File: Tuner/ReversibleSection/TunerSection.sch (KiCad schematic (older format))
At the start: 97 parts, among them J1 Conn_01x03, J10 Conn_01x02, J11 Conn_01x05, J12 Conn_01x01, J13 Conn_01x01, J14 Conn_01x01, J15 Conn_01x01, J2 Conn_01x03, J3 Conn_01x03, J4 Conn_01x03, J5 Conn_01x03, J6 Conn_01x03, J7 Conn_01x03, J8 Conn_01x02, J9 Conn_01x02, P10 Conn_01x01, P11 Conn_01x01, P12 Conn_01x01, P2 Conn_01x01, P3 Conn_01x01, P4 Conn_01x01, P5 Conn_01x01, P6 Conn_01x01, P7 Conn_01x01, P8 Conn_01x01, P9 Conn_01x01, U1 MCP23008, U2 ULN2803A

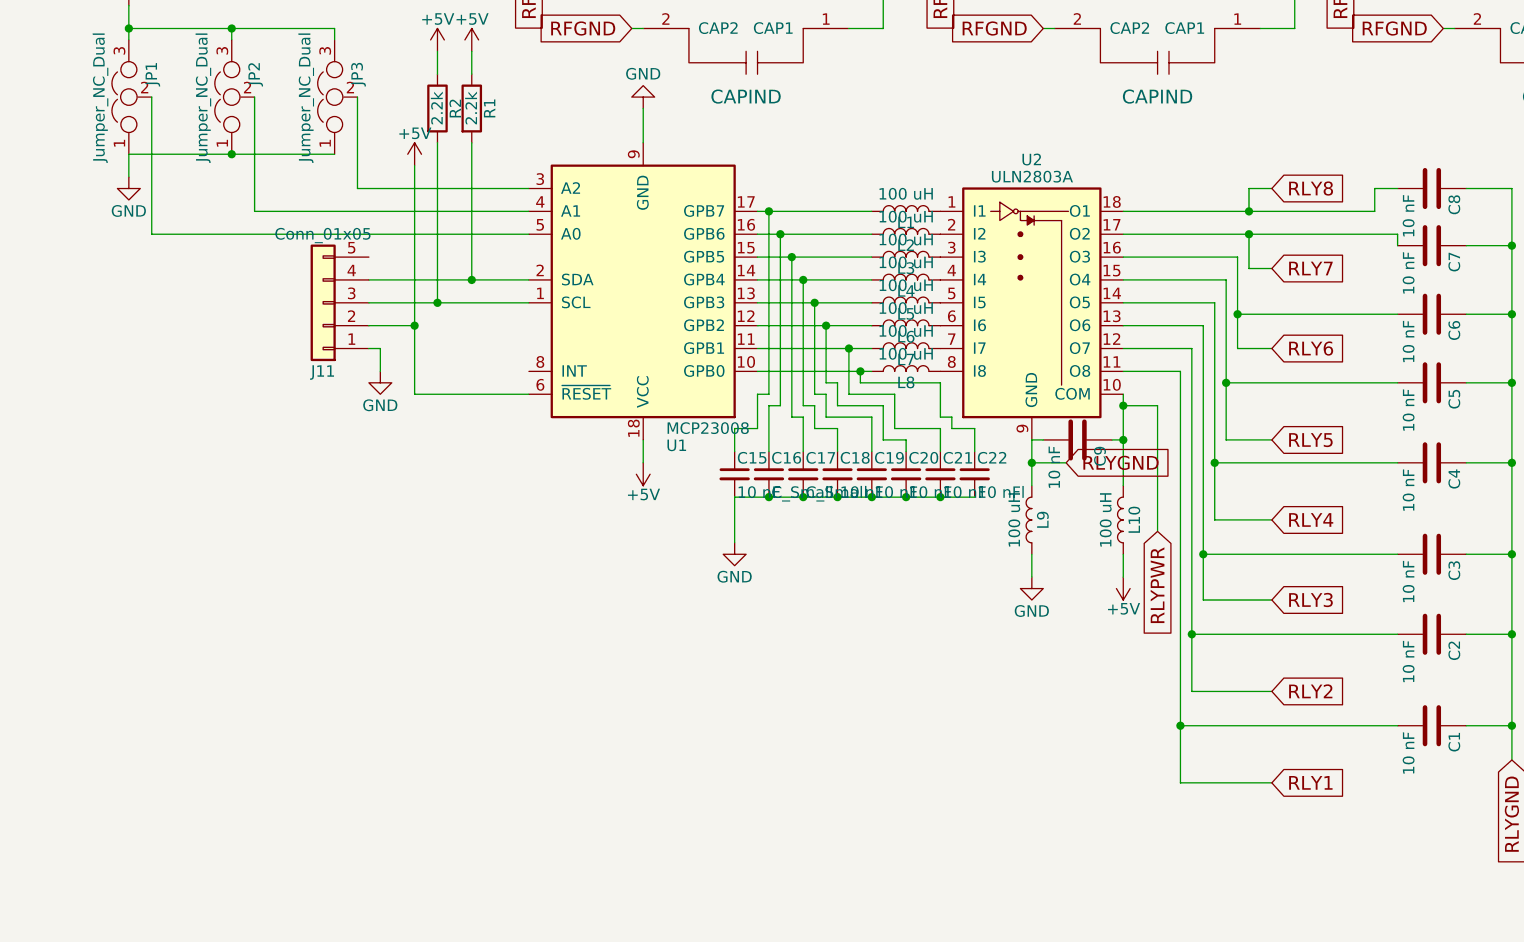
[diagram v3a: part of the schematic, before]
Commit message: JLCPCB order 09232018 - improved grounding - improved I2C cabling - NEO7M port - support for common mode chokes - relay board now has capacitors on all coils
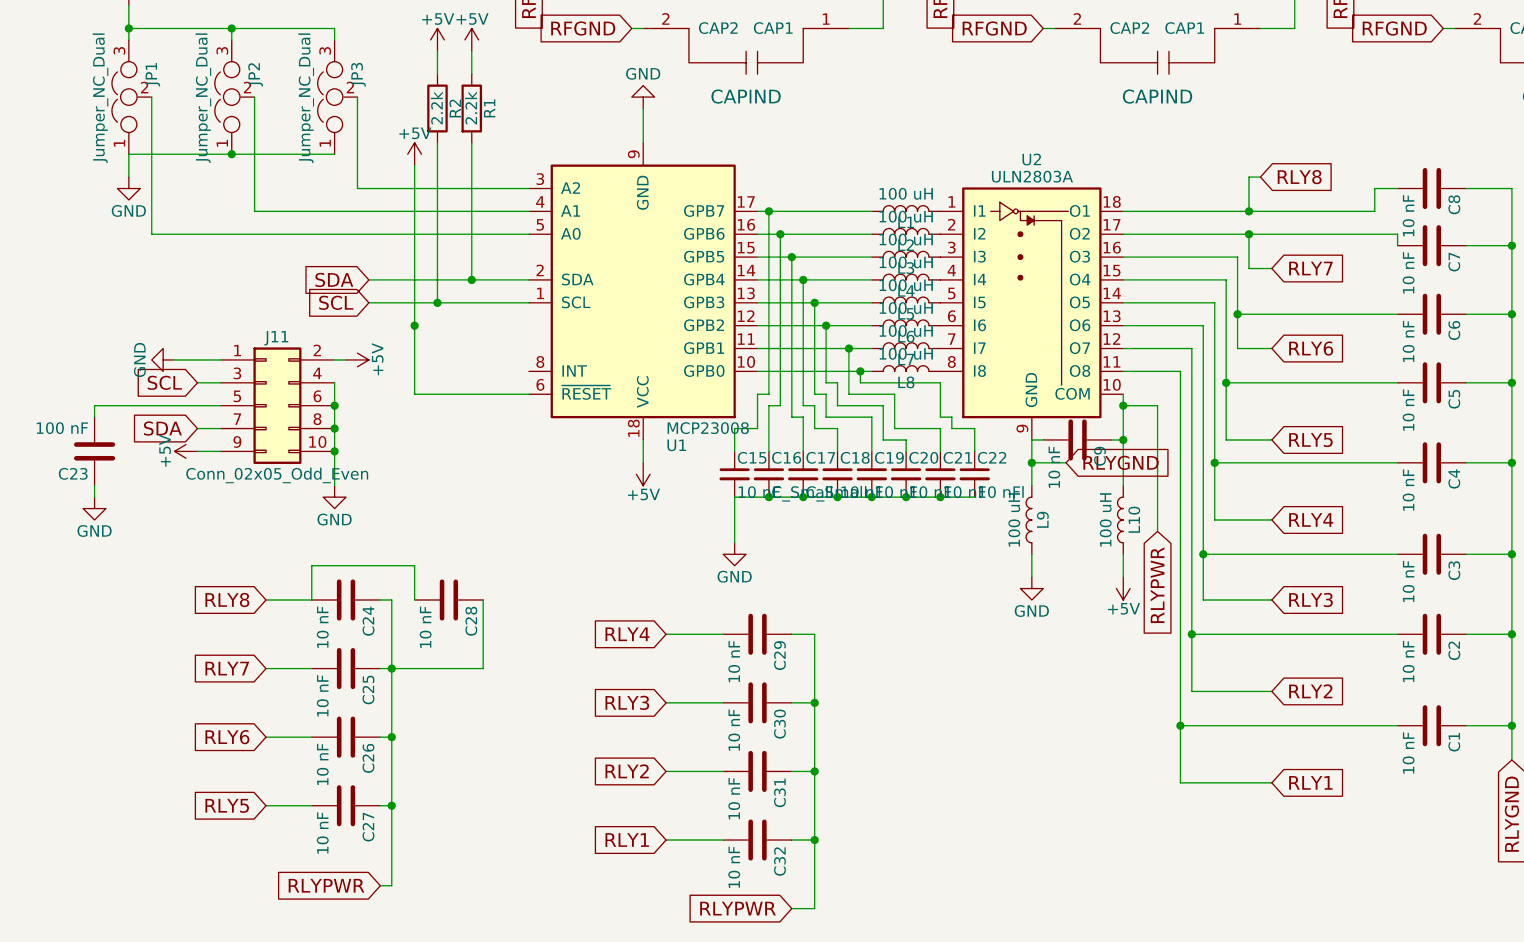
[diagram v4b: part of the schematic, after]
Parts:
- removed J11: Conn_01x05, Connectors_Molex:Molex_KK-6410-05_05x2.54mm_Straight, symbol Conn_01x05
- added C23: 100 nF, Capacitors_THT:C_Disc_D5.0mm_W2.5mm_P2.50mm, symbol C
- added C24, C25, C26, C27, C28, C29, C30, C31, C32: 10 nF, Capacitors_THT:C_Disc_D5.0mm_W2.5mm_P2.50mm, symbol C
- added J11: Conn_02x05_Odd_Even, Pin_Headers:Pin_Header_Straight_2x05_Pitch2.54mm, symbol Conn_02x05_Odd_Even
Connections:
- net +5V: now also J11.2 (Pin_2), J11.9 (Pin_9)
- net GND: now also C23.1, J11.1 (Pin_1), J11.10 (Pin_10), J11.4 (Pin_4), J11.6 (Pin_6), J11.8 (Pin_8)
- net RLY1: now also C32.2
- net RLY2: now also C31.2
- net RLY3: now also C30.2
- net RLY4: now also C29.2
- net RLY5: now also C27.2
- net RLY6: now also C26.2
- net RLY7: now also C25.2
- net RLY8: now also C24.2, C28.2
- net RLYPWR: now also C24.1, C25.1, C26.1, C27.1, C28.1, C29.1, C30.1, C31.1, C32.1
- net SCL: now reaches R2.2, U1.1 (SCL)
- net SCL: now also J11.3 (Pin_3)
- net SDA: now reaches R1.2, U1.2 (SDA)
- net SDA: now also J11.7 (Pin_7)
- new net: C23.2, J11.5 (Pin_5)

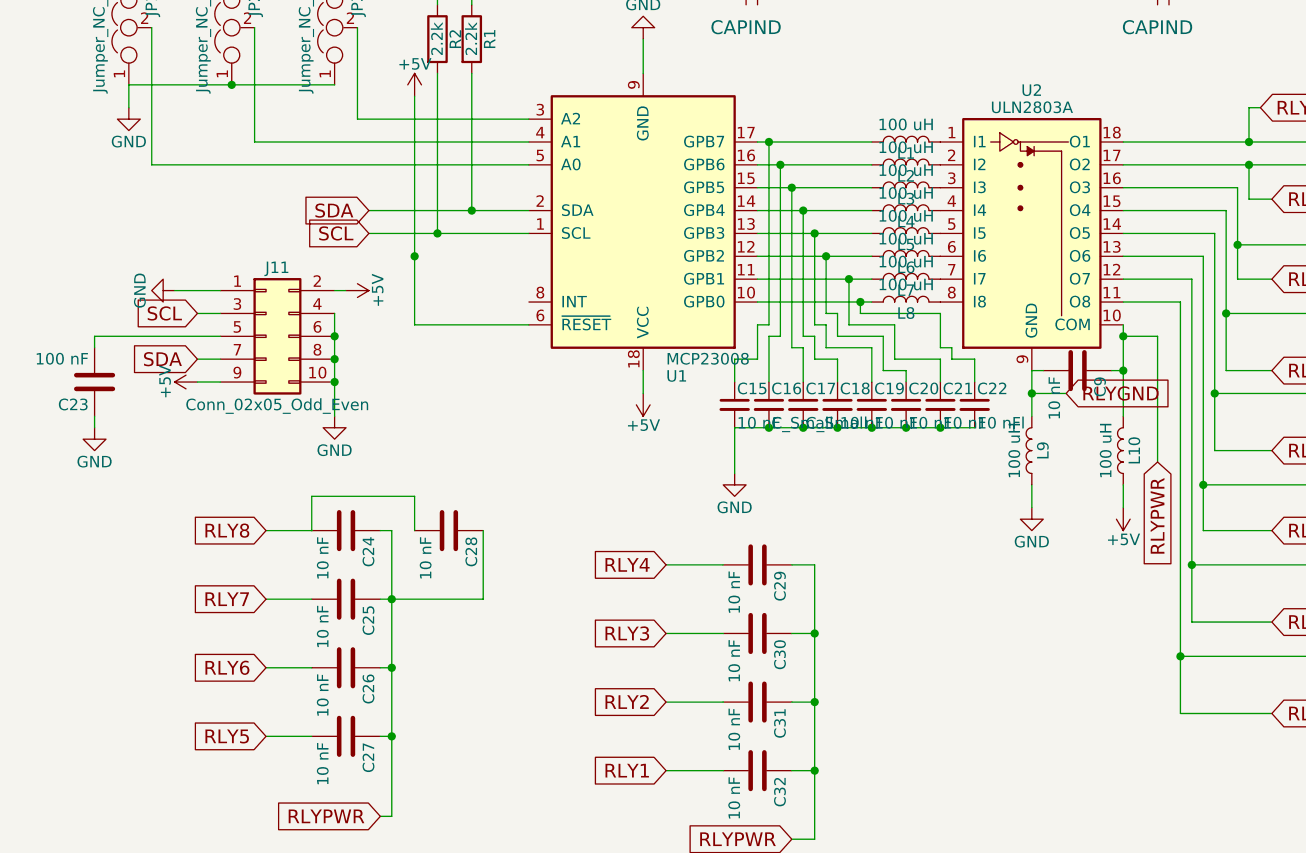
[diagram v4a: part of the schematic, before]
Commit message: Relay boards changed to have coil terminals all on same side
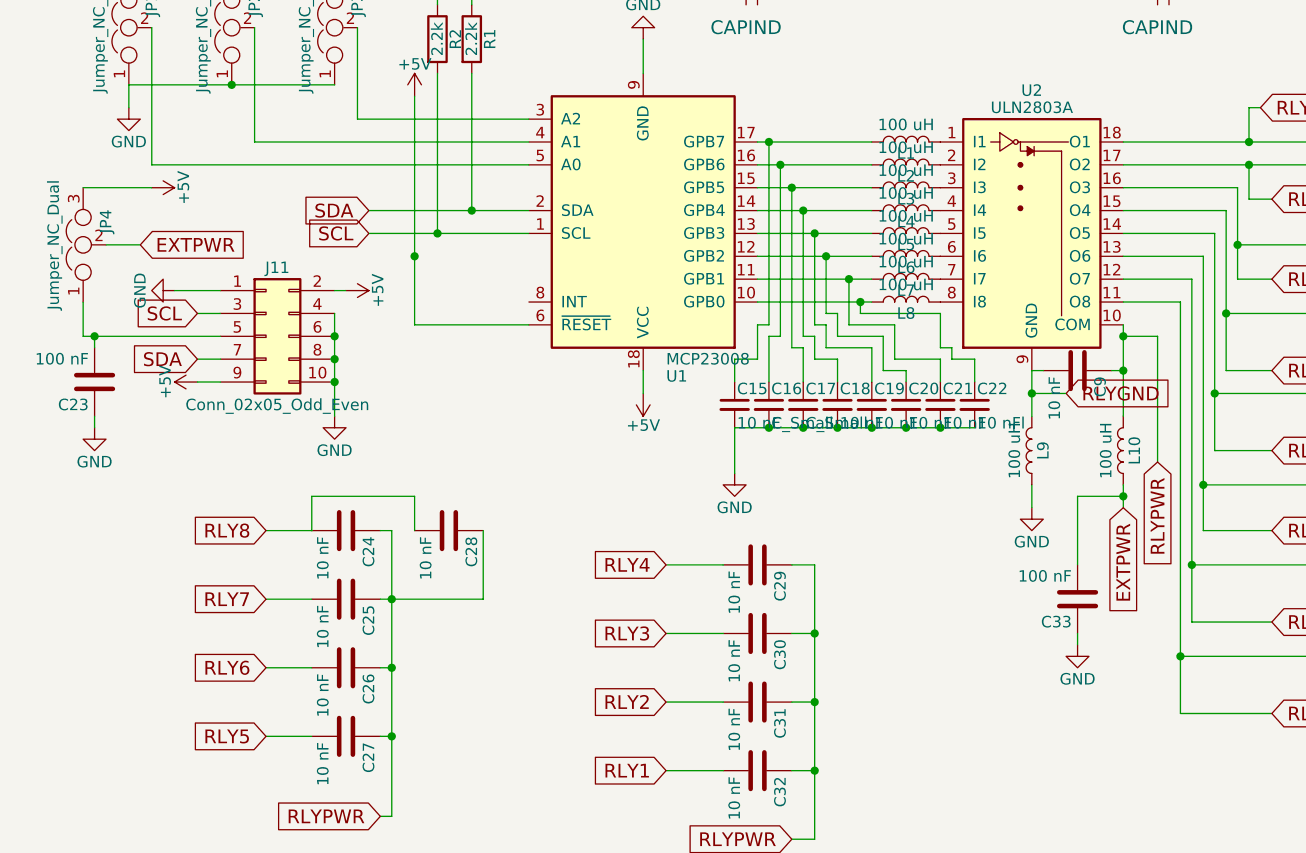
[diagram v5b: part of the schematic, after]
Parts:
- added C33: 100 nF, Capacitors_THT:C_Disc_D5.0mm_W2.5mm_P2.50mm, symbol C
- added JP4: Jumper_NC_Dual, Pin_Headers:Pin_Header_Straight_1x03_Pitch2.54mm, symbol Jumper_NC_Dual
- C11: footprint Capacitors_THT:CP_Radial_D8.0mm_P5.00mm -> Capacitors_THT:CP_Radial_Tantal_D5.0mm_P2.50mm
- C14, C9: footprint Capacitors_THT:C_Disc_D5.0mm_W2.5mm_P2.50mm -> Capacitors_THT:C_Disc_D5.0mm_W2.5mm_P5.00mm
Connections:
- net +5V: now also JP4.3; no longer L10.1
- net GND: now also C33.1
- net at C23.2, J11.5 (Pin_5): now also JP4.1
- new net EXTPWR: C33.2, JP4.2, L10.1
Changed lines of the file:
@@
 RLY8
 $Comp
-L +5V #PWR12
+L +5V #PWR13
 U 1 1 5B1A0287
 P 3150 5750
-F 0 "#PWR12" H 3150 5600 50  0001 C CNN
+F 0 "#PWR13" H 3150 5600 50  0001 C CNN
 F 1 "+5V" H 3150 5890 50  0000 C CNN
 F 2 "" H 3150 5750 50  0001 C CNN
@@
 $EndComp
 $Comp
-L +5V #PWR8
+L +5V #PWR9
 U 1 1 5B1ABA5A
 P 2150 4450
-F 0 "#PWR8" H 2150 4300 50  0001 C CNN
+F 0 "#PWR9" H 2150 4300 50  0001 C CNN
 F 1 "+5V" H 2150 4590 50  0000 C CNN
 F 2 "" H 2150 4450 50  0001 C CNN
@@
 $EndComp
 $Comp
-L +5V #PWR10
+L +5V #PWR11
 U 1 1 5B1ABCDE
 P 2400 3950
-F 0 "#PWR10" H 2400 3800 50  0001 C CNN
+F 0 "#PWR11" H 2400 3800 50  0001 C CNN
 F 1 "+5V" H 2400 4090 50  0000 C CNN
 F 2 "" H 2400 3950 50  0001 C CNN
@@
 $EndComp
 $Comp
-L +5V #PWR16
+L +5V #PWR17
 U 1 1 5B1ABFC6
 P 8800 4600
-F 0 "#PWR16" H 8800 4450 50  0001 C CNN
+F 0 "#PWR17" H 8800 4450 50  0001 C CNN
 F 1 "+5V" H 8800 4740 50  0000 C CNN
 F 2 "" H 8800 4600 50  0001 C CNN
@@
 $EndComp
 $Comp
-L GND #PWR17
+L GND #PWR18
 U 1 1 5B1AC04C
 P 8800 5050
-F 0 "#PWR17" H 8800 4800 50  0001 C CNN
+F 0 "#PWR18" H 8800 4800 50  0001 C CNN
 F 1 "GND" H 8800 4900 50  0000 C CNN
 F 2 "" H 8800 5050 50  0001 C CNN
@@
 F 0 "C11" H 9525 4950 50  0000 L CNN
 F 1 "100 uF" H 9525 4750 50  0000 L CNN
-F 2 "Capacitors_THT:CP_Radial_D8.0mm_P5.00mm" H 9538 4700 50  0001 C CNN
+F 2 "Capacitors_THT:CP_Radial_Tantal_D5.0mm_P2.50mm" H 9538 4700 50  0001 C CNN
 F 3 "" H 9500 4850 50  0001 C CNN
 	1    9500 4850
@@
 $EndComp
 $Comp
-L +5V #PWR9
+L +5V #PWR10
 U 1 1 5B196BCE
 P 2250 3950
-F 0 "#PWR9" H 2250 3800 50  0001 C CNN
+F 0 "#PWR10" H 2250 3800 50  0001 C CNN
 F 1 "+5V" H 2250 4090 50  0000 C CNN
 F 2 "" H 2250 3950 50  0001 C CNN
@@
 $EndComp
 $Comp
-L GND #PWR14
+L GND #PWR15
 U 1 1 5B9A4AE1
 P 4850 6250
-F 0 "#PWR14" H 4850 6000 50  0001 C CNN
+F 0 "#PWR15" H 4850 6000 50  0001 C CNN
 F 1 "GND" H 4850 6100 50  0000 C CNN
 F 2 "" H 4850 6250 50  0001 C CNN
@@
 	1    4850 6250
 	1    0    0    -1
-$EndComp
-$Comp
-L +5V #PWR15
-U 1 1 5B9A4F6D
-P 5250 6250
-F 0 "#PWR15" H 5250 6100 50  0001 C CNN
-F 1 "+5V" H 5250 6390 50  0000 C CNN
-F 2 "" H 5250 6250 50  0001 C CNN
-F 3 "" H 5250 6250 50  0001 C CNN
-	1    5250 6250
-	-1   0    0    1
 $EndComp
 $Comp
@@
 $EndComp
 $Comp
-L GND #PWR11
+L GND #PWR12
 U 1 1 5B9A6036
 P 3150 4200
-F 0 "#PWR11" H 3150 3950 50  0001 C CNN
+F 0 "#PWR12" H 3150 3950 50  0001 C CNN
 F 1 "GND" H 3150 4050 50  0000 C CNN
 F 2 "" H 3150 4200 50  0001 C CNN
@@
 $EndComp
 $Comp
-L GND #PWR13
+L GND #PWR14
 U 1 1 5B9ACA36
 P 3550 6100
-F 0 "#PWR13" H 3550 5850 50  0001 C CNN
+F 0 "#PWR14" H 3550 5850 50  0001 C CNN
 F 1 "GND" H 3550 5950 50  0000 C CNN
 F 2 "" H 3550 6100 50  0001 C CNN
@@
 F 0 "C9" H 5075 5750 50  0000 L CNN
 F 1 "10 nF" H 5075 5550 50  0000 L CNN
-F 2 "Capacitors_THT:C_Disc_D5.0mm_W2.5mm_P2.50mm" H 5088 5500 50  0001 C CNN
+F 2 "Capacitors_THT:C_Disc_D5.0mm_W2.5mm_P5.00mm" H 5088 5500 50  0001 C CNN
 F 3 "" H 5050 5650 50  0001 C CNN
 	1    5050 5650
@@
 $EndComp
 $Comp
-L GND #PWR18
+L GND #PWR19
 U 1 1 5B982525
 P 9850 2000
-F 0 "#PWR18" H 9850 1750 50  0001 C CNN
+F 0 "#PWR19" H 9850 1750 50  0001 C CNN
 F 1 "GND" H 9850 1850 50  0000 C CNN
 F 2 "" H 9850 2000 50  0001 C CNN
@@
 F 0 "C14" H 10175 2350 50  0000 L CNN
 F 1 "10 nF" H 10175 2150 50  0000 L CNN
-F 2 "Capacitors_THT:C_Disc_D5.0mm_W2.5mm_P2.50mm" H 10188 2100 50  0001 C CNN
+F 2 "Capacitors_THT:C_Disc_D5.0mm_W2.5mm_P5.00mm" H 10188 2100 50  0001 C CNN
 F 3 "" H 10150 2250 50  0001 C CNN
 	1    10150 2250
@@
 $EndComp
 $Comp
-L GND #PWR6
+L GND #PWR7
 U 1 1 5BA4D8F3
 P 1800 5850
-F 0 "#PWR6" H 1800 5600 50  0001 C CNN
+F 0 "#PWR7" H 1800 5600 50  0001 C CNN
 F 1 "GND" H 1800 5700 50  0000 C CNN
 F 2 "" H 1800 5850 50  0001 C CNN
@@
 $EndComp
 $Comp
-L +5V #PWR7
+L +5V #PWR8
 U 1 1 5BA4E273
 P 1850 5300
-F 0 "#PWR7" H 1850 5150 50  0001 C CNN
+F 0 "#PWR8" H 1850 5150 50  0001 C CNN
 F 1 "+5V" H 1850 5440 50  0000 C CNN
 F 2 "" H 1850 5300 50  0001 C CNN
@@
 $EndComp
 $Comp
-L +5V #PWR5
+L +5V #PWR6
 U 1 1 5BA4E663
 P 1200 5700
-F 0 "#PWR5" H 1200 5550 50  0001 C CNN
+F 0 "#PWR6" H 1200 5550 50  0001 C CNN
 F 1 "+5V" H 1200 5840 50  0000 C CNN
 F 2 "" H 1200 5700 50  0001 C CNN
@@
 $EndComp
 $Comp
-L GND #PWR4
+L GND #PWR5
 U 1 1 5BA5005D
 P 1100 5300
-F 0 "#PWR4" H 1100 5050 50  0001 C CNN
+F 0 "#PWR5" H 1100 5050 50  0001 C CNN
 F 1 "GND" H 1100 5150 50  0000 C CNN
 F 2 "" H 1100 5300 50  0001 C CNN
@@
 Text GLabel 3800 7700 0    60   Input ~ 0
 RLYPWR
+Text GLabel 5850 4500 2    60   Input ~ 0
+RLY8
+$Comp
+L Jumper_NC_Dual JP4
+U 1 1 5BAE44F6
+P 700 5100
+F 0 "JP4" H 750 5000 50  0000 L CNN
+F 1 "Jumper_NC_Dual" H 700 5200 50  0000 C BNN
+F 2 "Pin_Headers:Pin_Header_Straight_1x03_Pitch2.54mm" H 700 5100 50  0001 C CNN
+F 3 "" H 700 5100 50  0001 C CNN
+	1    700  5100
+	0    -1   -1   0
+$EndComp
+Text GLabel 950  5100 2    60   Input ~ 0
+EXTPWR
+$Comp
+L +5V #PWR4
+U 1 1 5BAE4DBC
+P 1000 4850
+F 0 "#PWR4" H 1000 4700 50  0001 C CNN
+F 1 "+5V" H 1000 4990 50  0000 C CNN
+F 2 "" H 1000 4850 50  0001 C CNN
+F 3 "" H 1000 4850 50  0001 C CNN
+	1    1000 4850
+	0    1    1    0
+$EndComp
+Text GLabel 5250 6250 3    60   Input ~ 0
+EXTPWR
+$Comp
+L C C33
+U 1 1 5BAED0CD
+P 5050 6650
+F 0 "C33" H 5075 6750 50  0000 L CNN
+F 1 "100 nF" H 5075 6550 50  0000 L CNN
+F 2 "Capacitors_THT:C_Disc_D5.0mm_W2.5mm_P2.50mm" H 5088 6500 50  0001 C CNN
+F 3 "" H 5050 6650 50  0001 C CNN
+	1    5050 6650
+	-1   0    0    1
+$EndComp
 Connection ~ 10200 5350
 Wire Wire Line
@@
 	750  5550 750  5500
 Wire Wire Line
-	750  5500 1300 5500
+	700  5500 1300 5500
 Wire Wire Line
 	1100 5300 1300 5300
@@
 	3900 7700 3800 7700
 Connection ~ 3900 7400
-Text GLabel 5850 4500 2    60   Input ~ 0
-RLY8
 Wire Wire Line
 	5800 4650 5800 4500
@@
 	5800 4500 5850 4500
 Connection ~ 5800 4650
+Wire Wire Line
+	700  5500 700  5350
+Connection ~ 750  5500
+Wire Wire Line
+	800  5100 950  5100
+Wire Wire Line
+	700  4850 1000 4850
+$Comp
+L GND #PWR16
+U 1 1 5BAEE216
+P 5050 6850
+F 0 "#PWR16" H 5050 6600 50  0001 C CNN
+F 1 "GND" H 5050 6700 50  0000 C CNN
+F 2 "" H 5050 6850 50  0001 C CNN
+F 3 "" H 5050 6850 50  0001 C CNN
+	1    5050 6850
+	1    0    0    -1
+$EndComp
+Wire Wire Line
+	5050 6800 5050 6850
+Wire Wire Line
+	5050 6500 5050 6200
+Wire Wire Line
+	5050 6200 5250 6200
+Connection ~ 5250 6200
 $EndSCHEMATC
